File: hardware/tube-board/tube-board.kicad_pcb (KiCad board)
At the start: 2 copper layers, 176 x 26 mm, 23 parts, among them J1 CONN_01X10, J2 CONN_01X10, U1 HV5522PG, U2 HV5522PG

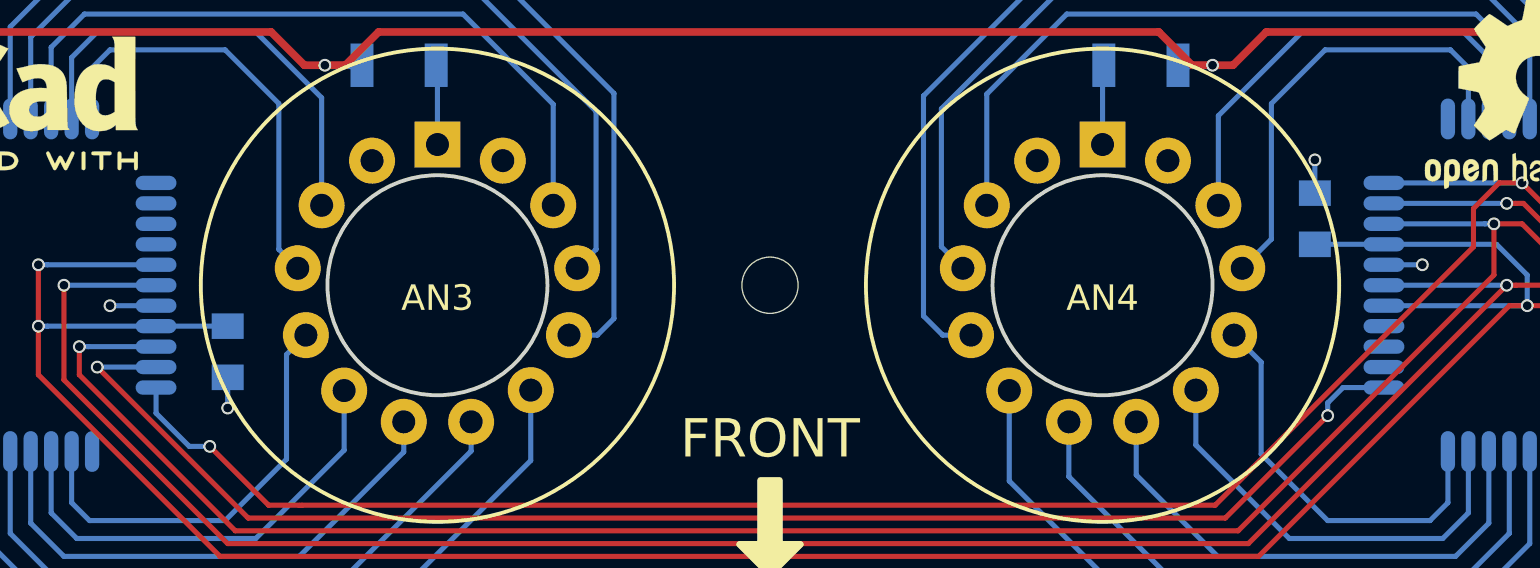
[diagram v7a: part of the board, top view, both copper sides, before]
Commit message: Switched to an 0603 capacitor on tube board
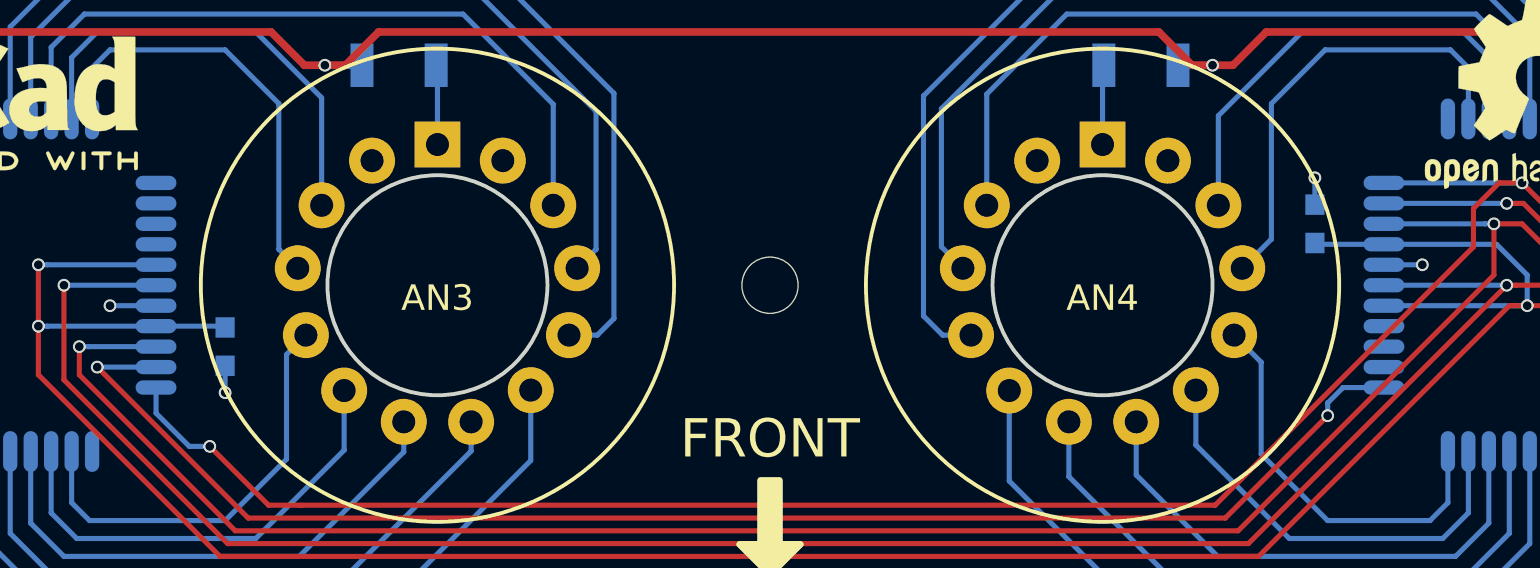
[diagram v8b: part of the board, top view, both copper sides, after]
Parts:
- C1, C2: footprint Capacitors_SMD:C_0805 -> Capacitors_SMD:C_0603
- moved C1 0.22 mm to (118.7, 107.4)
- moved C2 0.20 mm to (161.3, 102.6)
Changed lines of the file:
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@@
     (thickness 1.6)
     (drawings 11)
-    (tracks 529)
+    (tracks 531)
     (zones 0)
     (modules 23)
@@
     (fp_line (start -4.699 2.794) (end 0 -4.191) (layer F.SilkS) (width 0.381))
   )
-  (module Capacitors_SMD:C_0805 (layer B.Cu)
-    (at 118.8 107.6 270)
-    (descr "Capacitor SMD 0805, reflow soldering, AVX (see smccp.pdf)")
-    (tags "capacitor 0805")
-    (attr smd)
-    (fp_text reference C1 (at -2.5 0 360) (layer B.SilkS)
-      (effects (font (size 1 1) (thickness 0.15)) (justify mirror))
-    )
-    (fp_text value 0.1u (at 0 -1.75 270) (layer B.Fab)
-      (effects (font (size 1 1) (thickness 0.15)) (justify mirror))
-    )
-    (fp_text user %R (at 0 1.5 270) (layer B.Fab)
-      (effects (font (size 1 1) (thickness 0.15)) (justify mirror))
-    )
-    (fp_line (start -1 -0.62) (end -1 0.62) (layer B.Fab) (width 0.1))
-    (fp_line (start 1 -0.62) (end -1 -0.62) (layer B.Fab) (width 0.1))
-    (fp_line (start 1 0.62) (end 1 -0.62) (layer B.Fab) (width 0.1))
-    (fp_line (start -1 0.62) (end 1 0.62) (layer B.Fab) (width 0.1))
-    (fp_line (start 0.5 0.85) (end -0.5 0.85) (layer B.SilkS) (width 0.12))
-    (fp_line (start -0.5 -0.85) (end 0.5 -0.85) (layer B.SilkS) (width 0.12))
-    (fp_line (start -1.75 0.88) (end 1.75 0.88) (layer B.CrtYd) (width 0.05))
-    (fp_line (start -1.75 0.88) (end -1.75 -0.87) (layer B.CrtYd) (width 0.05))
-    (fp_line (start 1.75 -0.87) (end 1.75 0.88) (layer B.CrtYd) (width 0.05))
-    (fp_line (start 1.75 -0.87) (end -1.75 -0.87) (layer B.CrtYd) (width 0.05))
-    (pad 1 smd rect (at -1 0 270) (size 1 1.25) (layers B.Cu B.Paste B.Mask)
-      (net 79 +12V))
-    (pad 2 smd rect (at 1 0 270) (size 1 1.25) (layers B.Cu B.Paste B.Mask)
-      (net 80 GND))
-    (model Capacitors_SMD.3dshapes/C_0805.wrl
-      (at (xyz 0 0 0))
-      (scale (xyz 1 1 1))
-      (rotate (xyz 0 0 0))
-    )
-  )
-  (module Capacitors_SMD:C_0805 (layer B.Cu)
-    (at 161.3 102.4 90)
-    (descr "Capacitor SMD 0805, reflow soldering, AVX (see smccp.pdf)")
-    (tags "capacitor 0805")
-    (attr smd)
-    (fp_text reference C2 (at -2.6 0 180) (layer B.SilkS)
-      (effects (font (size 1 1) (thickness 0.15)) (justify mirror))
-    )
-    (fp_text value 0.1u (at 0 -1.75 90) (layer B.Fab)
-      (effects (font (size 1 1) (thickness 0.15)) (justify mirror))
-    )
-    (fp_text user %R (at 0 1.5 90) (layer B.Fab)
-      (effects (font (size 1 1) (thickness 0.15)) (justify mirror))
-    )
-    (fp_line (start -1 -0.62) (end -1 0.62) (layer B.Fab) (width 0.1))
-    (fp_line (start 1 -0.62) (end -1 -0.62) (layer B.Fab) (width 0.1))
-    (fp_line (start 1 0.62) (end 1 -0.62) (layer B.Fab) (width 0.1))
-    (fp_line (start -1 0.62) (end 1 0.62) (layer B.Fab) (width 0.1))
-    (fp_line (start 0.5 0.85) (end -0.5 0.85) (layer B.SilkS) (width 0.12))
-    (fp_line (start -0.5 -0.85) (end 0.5 -0.85) (layer B.SilkS) (width 0.12))
-    (fp_line (start -1.75 0.88) (end 1.75 0.88) (layer B.CrtYd) (width 0.05))
-    (fp_line (start -1.75 0.88) (end -1.75 -0.87) (layer B.CrtYd) (width 0.05))
-    (fp_line (start 1.75 -0.87) (end 1.75 0.88) (layer B.CrtYd) (width 0.05))
-    (fp_line (start 1.75 -0.87) (end -1.75 -0.87) (layer B.CrtYd) (width 0.05))
-    (pad 1 smd rect (at -1 0 90) (size 1 1.25) (layers B.Cu B.Paste B.Mask)
-      (net 79 +12V))
-    (pad 2 smd rect (at 1 0 90) (size 1 1.25) (layers B.Cu B.Paste B.Mask)
-      (net 80 GND))
-    (model Capacitors_SMD.3dshapes/C_0805.wrl
-      (at (xyz 0 0 0))
-      (scale (xyz 1 1 1))
-      (rotate (xyz 0 0 0))
-    )
-  )
   (module Symbols:OSHW-Logo2_9.8x8mm_SilkScreen (layer F.Cu)
     (at 170 97.5)
@@
     (pad 13 thru_hole circle (at 2.555977 -4.870008 332.3077) (size 1.8 1.8) (drill 0.9) (layers *.Cu *.Mask)
       (net 78 "Net-(AN6-Pad13)"))
+  )
+  (module Capacitors_SMD:C_0603 (layer B.Cu)
+    (at 118.7 107.4 270)
+    (descr "Capacitor SMD 0603, reflow soldering, AVX (see smccp.pdf)")
+    (tags "capacitor 0603")
+    (attr smd)
+    (fp_text reference C1 (at 0 1.5 270) (layer B.SilkS)
+      (effects (font (size 1 1) (thickness 0.15)) (justify mirror))
+    )
+    (fp_text value 0.1u (at 0 -1.5 270) (layer B.Fab)
+      (effects (font (size 1 1) (thickness 0.15)) (justify mirror))
+    )
+    (fp_text user %R (at 0 1.5 270) (layer B.Fab)
+      (effects (font (size 1 1) (thickness 0.15)) (justify mirror))
+    )
+    (fp_line (start -0.8 -0.4) (end -0.8 0.4) (layer B.Fab) (width 0.1))
+    (fp_line (start 0.8 -0.4) (end -0.8 -0.4) (layer B.Fab) (width 0.1))
+    (fp_line (start 0.8 0.4) (end 0.8 -0.4) (layer B.Fab) (width 0.1))
+    (fp_line (start -0.8 0.4) (end 0.8 0.4) (layer B.Fab) (width 0.1))
+    (fp_line (start -0.35 0.6) (end 0.35 0.6) (layer B.SilkS) (width 0.12))
+    (fp_line (start 0.35 -0.6) (end -0.35 -0.6) (layer B.SilkS) (width 0.12))
+    (fp_line (start -1.4 0.65) (end 1.4 0.65) (layer B.CrtYd) (width 0.05))
+    (fp_line (start -1.4 0.65) (end -1.4 -0.65) (layer B.CrtYd) (width 0.05))
+    (fp_line (start 1.4 -0.65) (end 1.4 0.65) (layer B.CrtYd) (width 0.05))
+    (fp_line (start 1.4 -0.65) (end -1.4 -0.65) (layer B.CrtYd) (width 0.05))
+    (pad 1 smd rect (at -0.75 0 270) (size 0.8 0.75) (layers B.Cu B.Paste B.Mask)
+      (net 79 +12V))
+    (pad 2 smd rect (at 0.75 0 270) (size 0.8 0.75) (layers B.Cu B.Paste B.Mask)
+      (net 80 GND))
+    (model Capacitors_SMD.3dshapes/C_0603.wrl
+      (at (xyz 0 0 0))
+      (scale (xyz 1 1 1))
+      (rotate (xyz 0 0 0))
+    )
+  )
+  (module Capacitors_SMD:C_0603 (layer B.Cu)
+    (at 161.3 102.6 90)
+    (descr "Capacitor SMD 0603, reflow soldering, AVX (see smccp.pdf)")
+    (tags "capacitor 0603")
+    (attr smd)
+    (fp_text reference C2 (at 0 1.5 90) (layer B.SilkS)
+      (effects (font (size 1 1) (thickness 0.15)) (justify mirror))
+    )
+    (fp_text value 0.1u (at 0 -1.5 90) (layer B.Fab)
+      (effects (font (size 1 1) (thickness 0.15)) (justify mirror))
+    )
+    (fp_text user %R (at 0 1.5 90) (layer B.Fab)
+      (effects (font (size 1 1) (thickness 0.15)) (justify mirror))
+    )
+    (fp_line (start -0.8 -0.4) (end -0.8 0.4) (layer B.Fab) (width 0.1))
+    (fp_line (start 0.8 -0.4) (end -0.8 -0.4) (layer B.Fab) (width 0.1))
+    (fp_line (start 0.8 0.4) (end 0.8 -0.4) (layer B.Fab) (width 0.1))
+    (fp_line (start -0.8 0.4) (end 0.8 0.4) (layer B.Fab) (width 0.1))
+    (fp_line (start -0.35 0.6) (end 0.35 0.6) (layer B.SilkS) (width 0.12))
+    (fp_line (start 0.35 -0.6) (end -0.35 -0.6) (layer B.SilkS) (width 0.12))
+    (fp_line (start -1.4 0.65) (end 1.4 0.65) (layer B.CrtYd) (width 0.05))
+    (fp_line (start -1.4 0.65) (end -1.4 -0.65) (layer B.CrtYd) (width 0.05))
+    (fp_line (start 1.4 -0.65) (end 1.4 0.65) (layer B.CrtYd) (width 0.05))
+    (fp_line (start 1.4 -0.65) (end -1.4 -0.65) (layer B.CrtYd) (width 0.05))
+    (pad 1 smd rect (at -0.75 0 90) (size 0.8 0.75) (layers B.Cu B.Paste B.Mask)
+      (net 79 +12V))
+    (pad 2 smd rect (at 0.75 0 90) (size 0.8 0.75) (layers B.Cu B.Paste B.Mask)
+      (net 80 GND))
+    (model Capacitors_SMD.3dshapes/C_0603.wrl
+      (at (xyz 0 0 0))
+      (scale (xyz 1 1 1))
+      (rotate (xyz 0 0 0))
+    )
   )
   (gr_text FRONT (at 140 111) (layer F.SilkS)
@@
   (segment (start 157.5 115.6) (end 166.8 115.6) (width 0.2) (layer B.Cu) (net 77))
   (segment (start 166.8 115.6) (end 168.1 114.3) (width 0.2) (layer B.Cu) (net 77))
+  (segment (start 164 103.4) (end 161.35 103.4) (width 0.2) (layer B.Cu) (net 79))
+  (segment (start 161.35 103.4) (end 161.3 103.35) (width 0.2) (layer B.Cu) (net 79))
+  (segment (start 116 106.6) (end 118.65 106.6) (width 0.2) (layer B.Cu) (net 79))
+  (segment (start 118.65 106.6) (end 118.7 106.65) (width 0.2) (layer B.Cu) (net 79))
   (segment (start 168.4 103.4) (end 164 103.4) (width 0.2) (layer B.Cu) (net 79))
   (segment (start 169.246447 105.8) (end 164 105.8) (width 0.2) (layer B.Cu) (net 79))
-  (segment (start 161.3 103.4) (end 164 103.4) (width 0.2) (layer B.Cu) (net 79))
   (segment (start 111.4 104.2) (end 111.753553 104.2) (width 0.2) (layer B.Cu) (net 79))
   (segment (start 111.753553 104.2) (end 116 104.2) (width 0.2) (layer B.Cu) (net 79))
-  (segment (start 116 106.6) (end 118.8 106.6) (width 0.2) (layer B.Cu) (net 79))
   (segment (start 111.753553 106.6) (end 116 106.6) (width 0.2) (layer B.Cu) (net 79))
   (segment (start 197.5 100.5) (end 198.1 101.1) (width 0.2) (layer F.Cu) (net 79))
@@
   (via (at 197.5 100.5) (size 0.5) (drill 0.34) (layers F.Cu B.Cu) (net 79))
   (segment (start 197.555 100.555) (end 197.5 100.5) (width 0.2) (layer B.Cu) (net 79))
+  (segment (start 161.3 101.85) (end 161.3 100.8) (width 0.2) (layer B.Cu) (net 80))
+  (via (at 161.3 100.8) (size 0.5) (drill 0.34) (layers F.Cu B.Cu) (net 80))
+  (segment (start 118.7 108.15) (end 118.7 109.2) (width 0.2) (layer B.Cu) (net 80))
+  (via (at 118.7 109.2) (size 0.5) (drill 0.34) (layers F.Cu B.Cu) (net 80))
   (segment (start 164 104.2) (end 165.5 104.2) (width 0.2) (layer B.Cu) (net 80))
   (via (at 165.5 104.2) (size 0.5) (drill 0.34) (layers F.Cu B.Cu) (net 80))
-  (segment (start 161.3 101.4) (end 161.3 100.1) (width 0.2) (layer B.Cu) (net 80))
-  (via (at 161.3 100.1) (size 0.5) (drill 0.34) (layers F.Cu B.Cu) (net 80))
-  (segment (start 118.8 108.6) (end 118.8 109.8) (width 0.2) (layer B.Cu) (net 80))
-  (via (at 118.8 109.8) (size 0.5) (drill 0.34) (layers F.Cu B.Cu) (net 80))
   (segment (start 116 105.8) (end 114.2 105.8) (width 0.2) (layer B.Cu) (net 80))
   (via (at 114.2 105.8) (size 0.5) (drill 0.34) (layers F.Cu B.Cu) (net 80))
